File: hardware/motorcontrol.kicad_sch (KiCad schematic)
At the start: 25 parts, among them IC3 DRV8214RTER, IC4 DRV8214RTER, IC5 DRV8214RTER, IC6 DRV8214RTER, IC7 DRV8214RTER

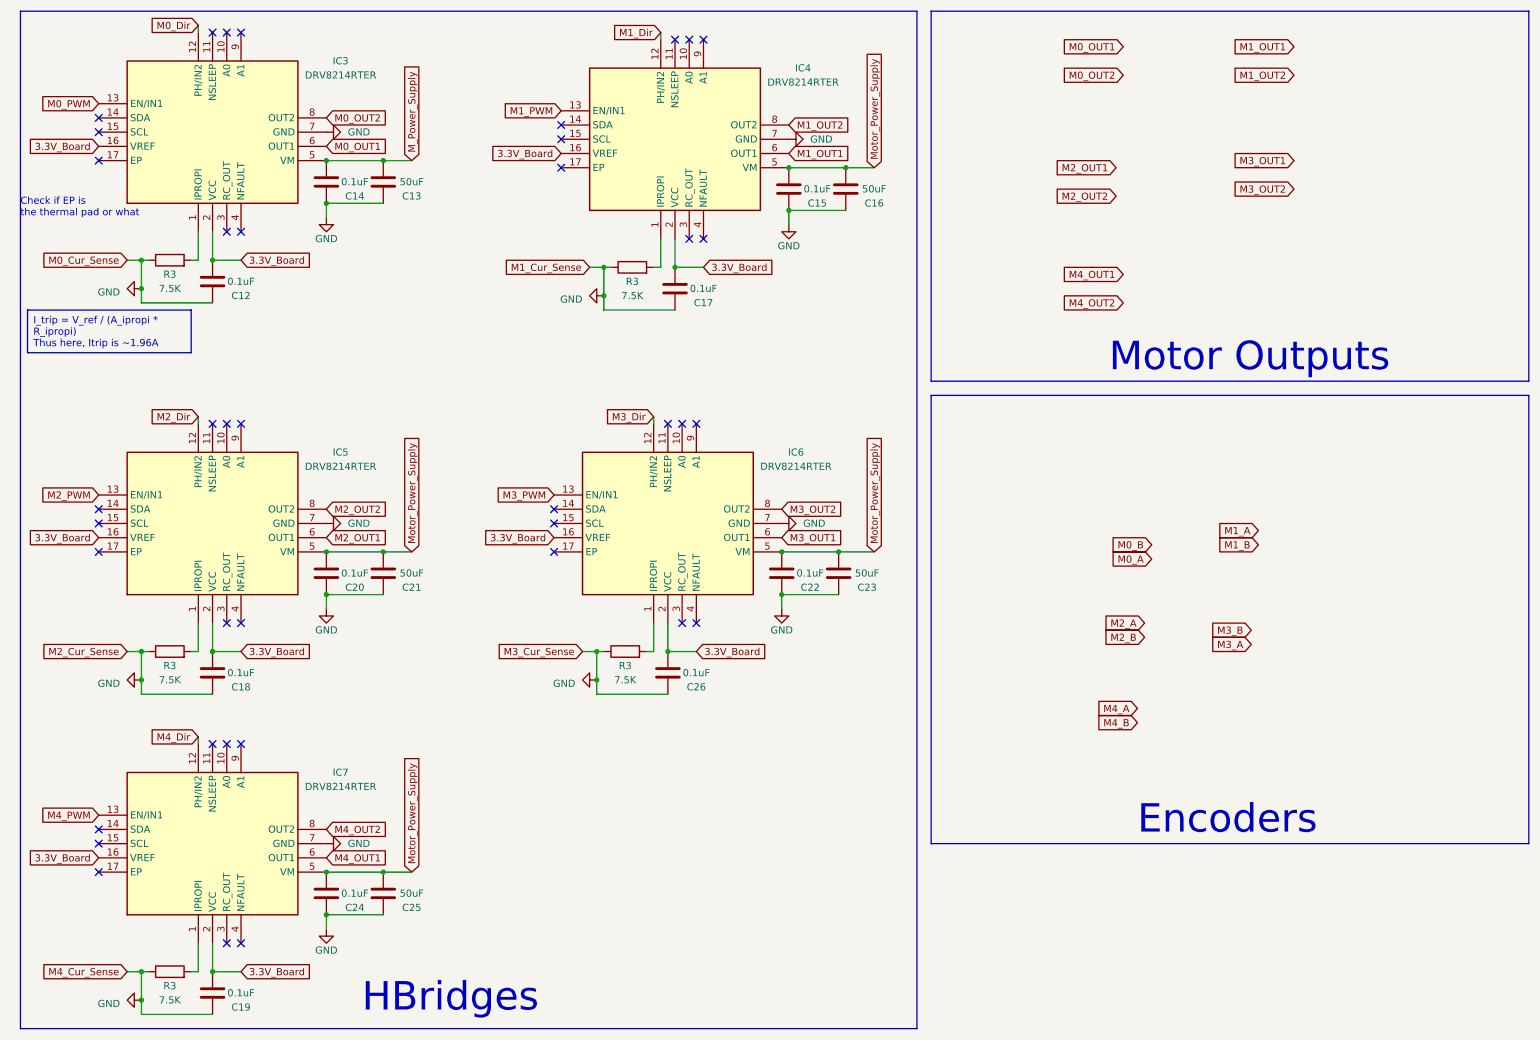
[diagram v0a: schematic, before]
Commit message: Change STM code to support an I2C bus. Add encoder reading code - tested on TIM1.
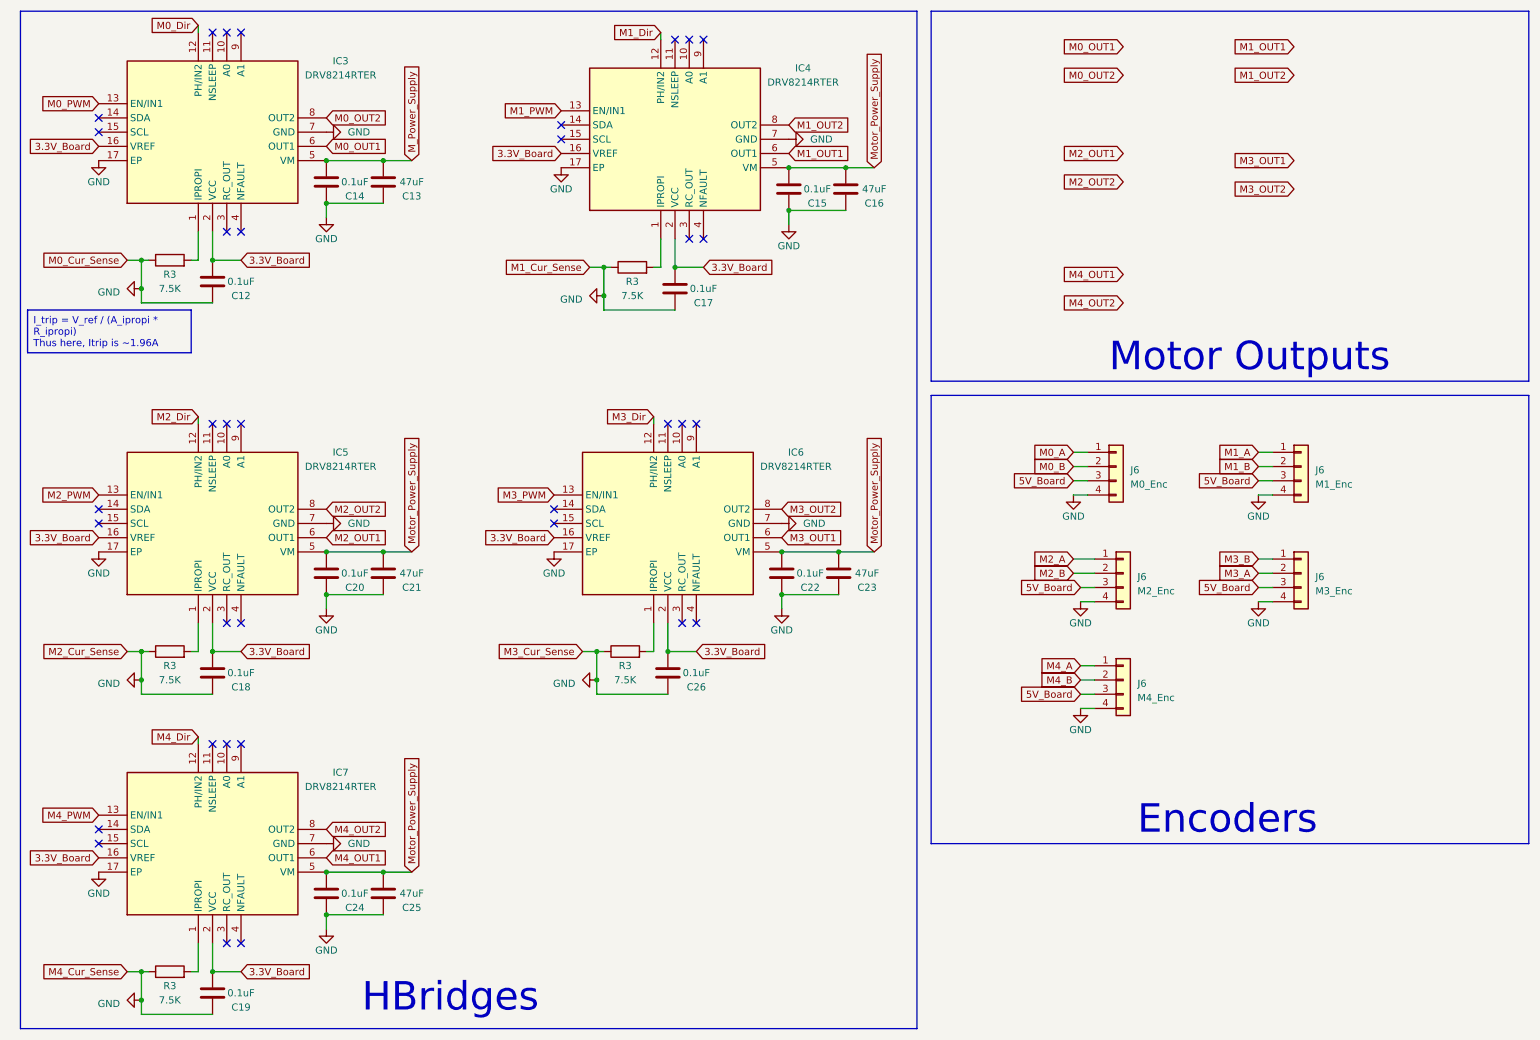
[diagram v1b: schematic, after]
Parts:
- added J6: M1_Enc, Connector_JST:JST_PH_B4B-PH-K_1x04_P2.00mm_Vertical, symbol Connector_Generic:Conn_01x04
- added J6: M3_Enc, Connector_JST:JST_PH_B4B-PH-K_1x04_P2.00mm_Vertical, symbol Connector_Generic:Conn_01x04
- added J6: M0_Enc, Connector_JST:JST_PH_B4B-PH-K_1x04_P2.00mm_Vertical, symbol Connector_Generic:Conn_01x04
- added J6: M2_Enc, Connector_JST:JST_PH_B4B-PH-K_1x04_P2.00mm_Vertical, symbol Connector_Generic:Conn_01x04
- added J6: M4_Enc, Connector_JST:JST_PH_B4B-PH-K_1x04_P2.00mm_Vertical, symbol Connector_Generic:Conn_01x04
- C13, C16, C21, C23, C25: value 50uF -> 47uF; footprint Capacitor_SMD:C_0402_1005Metric -> Capacitor_SMD:C_0805_2012Metric
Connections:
- net GND: now also IC3.17 (EP), IC4.17 (EP), IC5.17 (EP), IC6.17 (EP), IC7.17 (EP), J6.4 (Pin_4), J6.4 (Pin_4), J6.4 (Pin_4), J6.4 (Pin_4), J6.4 (Pin_4)
- net M0_A: now also J6.1 (Pin_1)
- net M0_B: now also J6.2 (Pin_2)
- net M1_A: now also J6.1 (Pin_1)
- net M1_B: now also J6.2 (Pin_2)
- net M2_A: now also J6.1 (Pin_1)
- net M2_B: now also J6.2 (Pin_2)
- net M3_A: now also J6.2 (Pin_2)
- net M3_B: now also J6.1 (Pin_1)
- net M4_A: now also J6.1 (Pin_1)
- net M4_B: now also J6.2 (Pin_2)
- new net 5V_Board: J6.3 (Pin_3), J6.3 (Pin_3), J6.3 (Pin_3), J6.3 (Pin_3), J6.3 (Pin_3)
- no-connect marks 40 -> 35
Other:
- note removed: "Check if EP is the thermal pad or what"

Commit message: Add past project scripts. Add more lib components.
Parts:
- added J13, J14, J15, J16, J17: 1729128, SamacSys_Parts:1729128, symbol SamacSys_Parts:1729128
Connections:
- net 3.3V_Board: now also IC5.10 (A0)
- net GND: now also IC3.10 (A0), IC3.9 (A1), IC4.9 (A1), IC5.9 (A1), IC6.10 (A0)
- net M0_OUT1: now also J14.1
- net M0_OUT2: now also J14.2
- net M1_OUT1: now also J13.1
- net M1_OUT2: now also J13.2
- net M2_OUT1: now also J15.1
- net M2_OUT2: now also J15.2
- net M3_OUT1: now also J16.1
- net M3_OUT2: now also J16.2
- net M4_OUT1: now also J17.1
- net M4_OUT2: now also J17.2
- net I2C_SDA: now reaches IC7.14 (SDA)
- net I2C_SDA: now also IC3.14 (SDA), IC4.14 (SDA), IC5.14 (SDA), IC6.14 (SDA)
- net I2C_SCL: now reaches IC7.15 (SCL)
- net I2C_SCL: now also IC3.15 (SCL), IC4.15 (SCL), IC5.15 (SCL), IC6.15 (SCL)
- net M0_Dir: no longer names the net of IC3.12 (PH/IN2)
- net M0_PWM: no longer names the net of IC3.13 (EN/IN1)
- net M1_Dir: no longer names the net of IC4.12 (PH/IN2)
- net M1_PWM: no longer names the net of IC4.13 (EN/IN1)
- net M2_Dir: no longer names the net of IC5.12 (PH/IN2)
- net M2_PWM: no longer names the net of IC5.13 (EN/IN1)
- net M3_Dir: no longer names the net of IC6.12 (PH/IN2)
- net M3_PWM: no longer names the net of IC6.13 (EN/IN1)
- net M4_Dir: no longer names the net of IC7.12 (PH/IN2)
- net M4_PWM: no longer names the net of IC7.13 (EN/IN1)
- no-connect marks 35 -> 29
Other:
- moved on the sheet: J6
